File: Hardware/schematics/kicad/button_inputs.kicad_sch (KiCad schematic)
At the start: 28 parts, among them SW1 ENC_A, SW2 ENC_B, SW3 ENC_BUT, SW4 AUTOTUNE_BTN, SW5 OFFSET_RESET, SW6 OFFSET_DISPLAY, SW7 OSC1_THROUGH, SW8 LOAD_SD, U15 74HC595, U16 74HC595, U17 74HC595, U27 74HC165

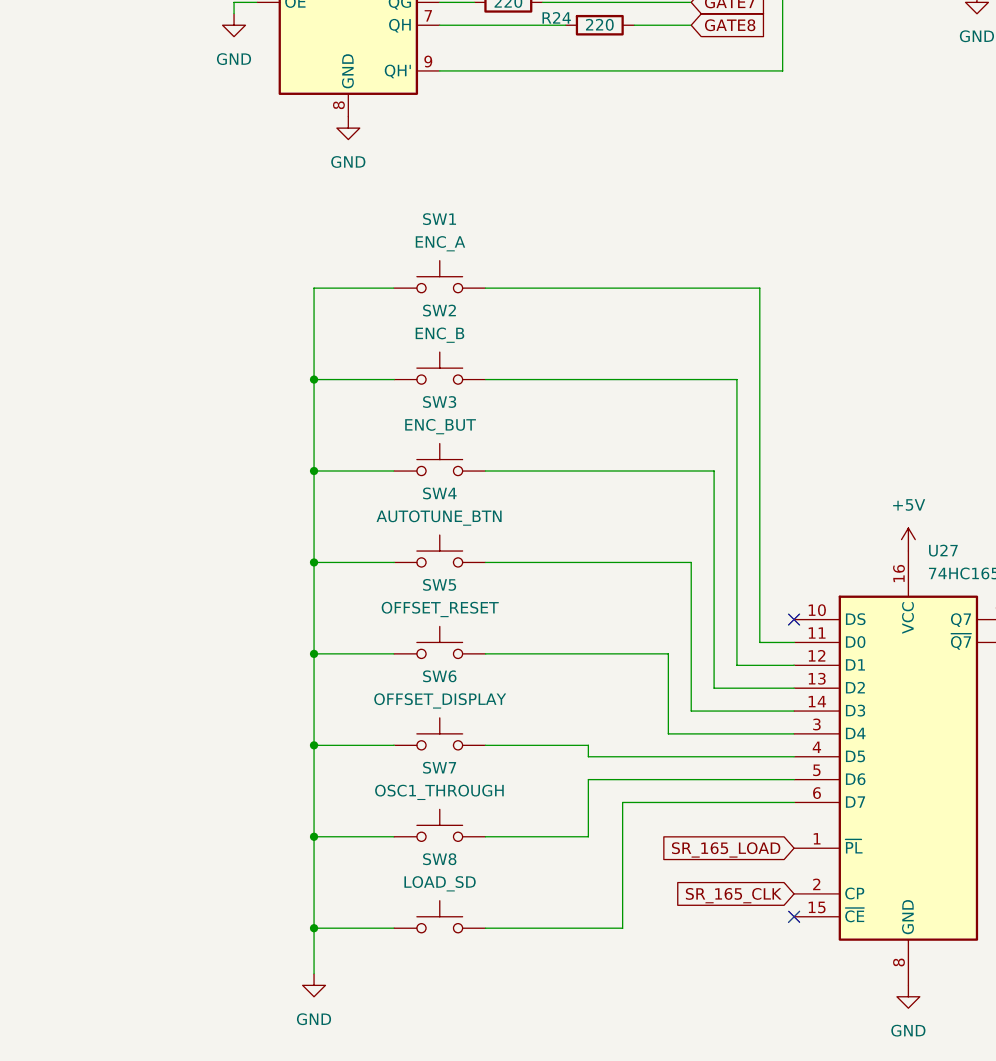
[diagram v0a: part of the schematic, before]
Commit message: Add 3.3v pull-up resistors to buttons
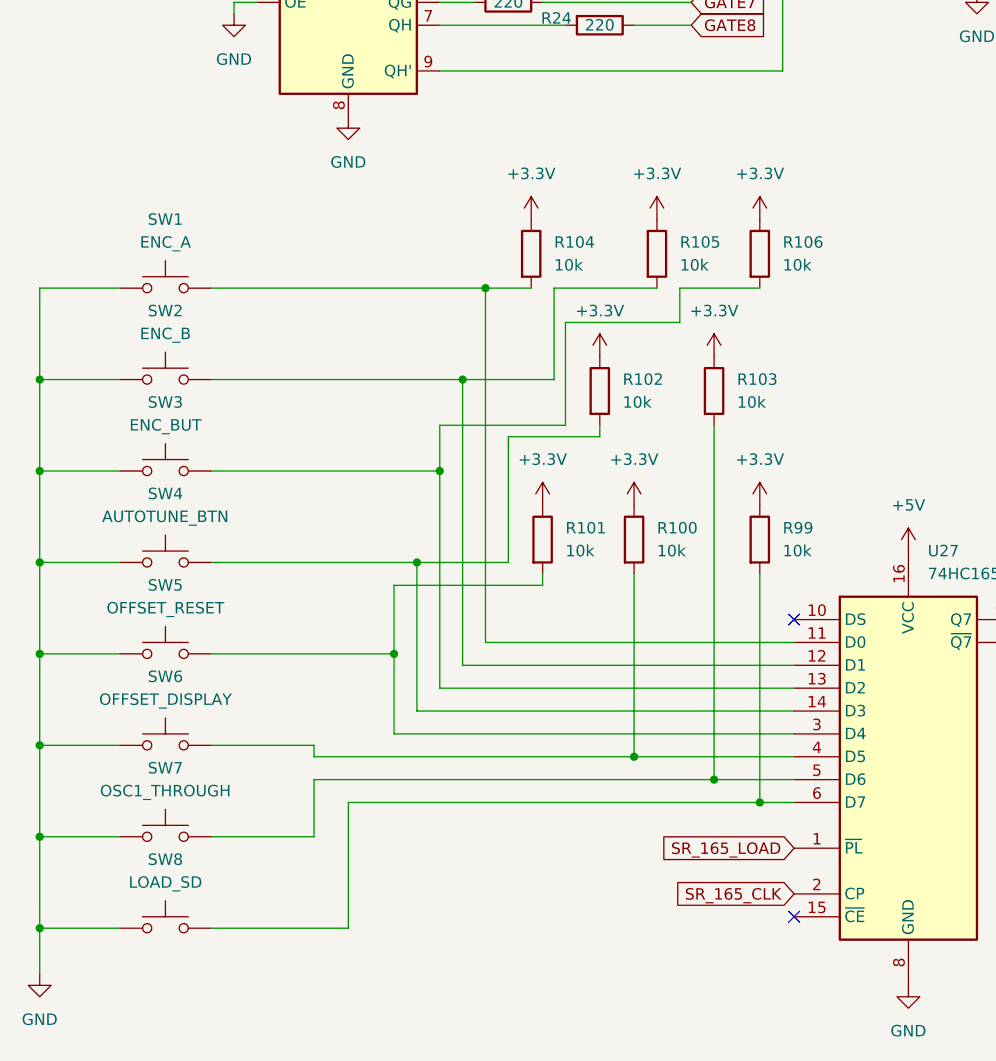
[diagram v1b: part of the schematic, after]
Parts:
- added R100, R101, R102, R103, R104, R105, R106, R99: 10k, symbol Device:R
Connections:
- net at SW1.2, U27.11 (D0): now also R104.2
- net at SW2.2, U27.12 (D1): now also R105.2
- net at SW3.2, U27.13 (D2): now also R106.2
- net at SW4.2, U27.14 (D3): now also R102.2
- net at SW5.2, U27.3 (D4): now also R101.2
- net at SW6.2, U27.4 (D5): now also R100.2
- net at SW7.2, U27.5 (D6): now also R103.2
- net at SW8.2, U27.6 (D7): now also R99.2
- new net +3.3V: R100.1, R101.1, R102.1, R103.1, R104.1, R105.1, R106.1, R99.1
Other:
- moved on the sheet: SW1, SW2, SW3, SW4, SW5, SW6, SW7, SW8

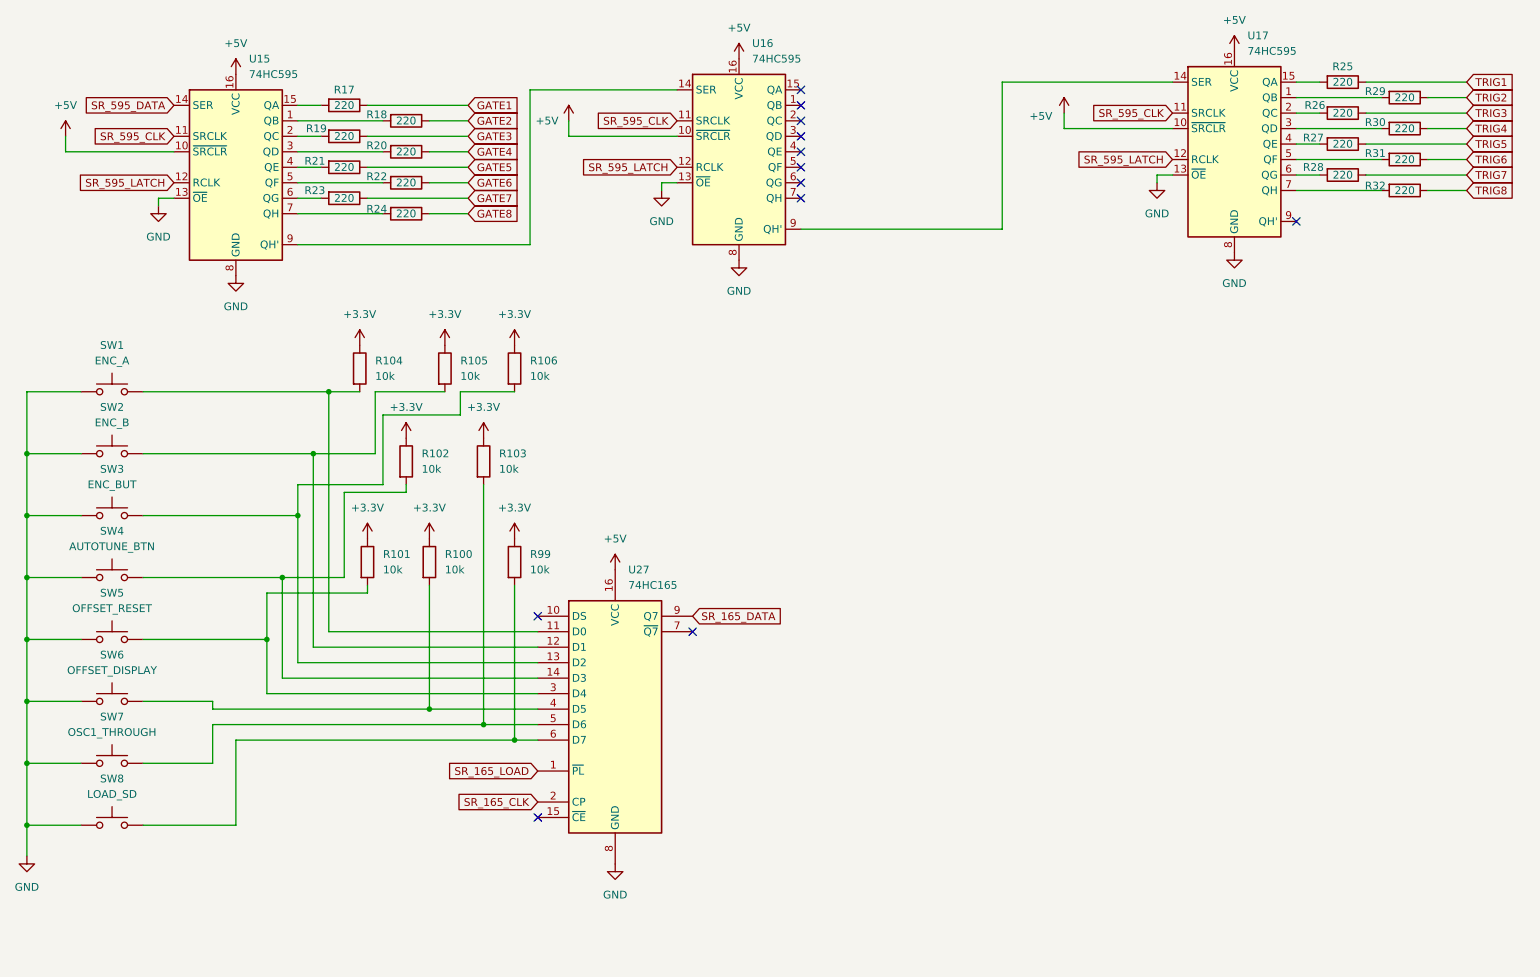
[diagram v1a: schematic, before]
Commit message: Modify schematics to suit a complete Eurorack PCB design
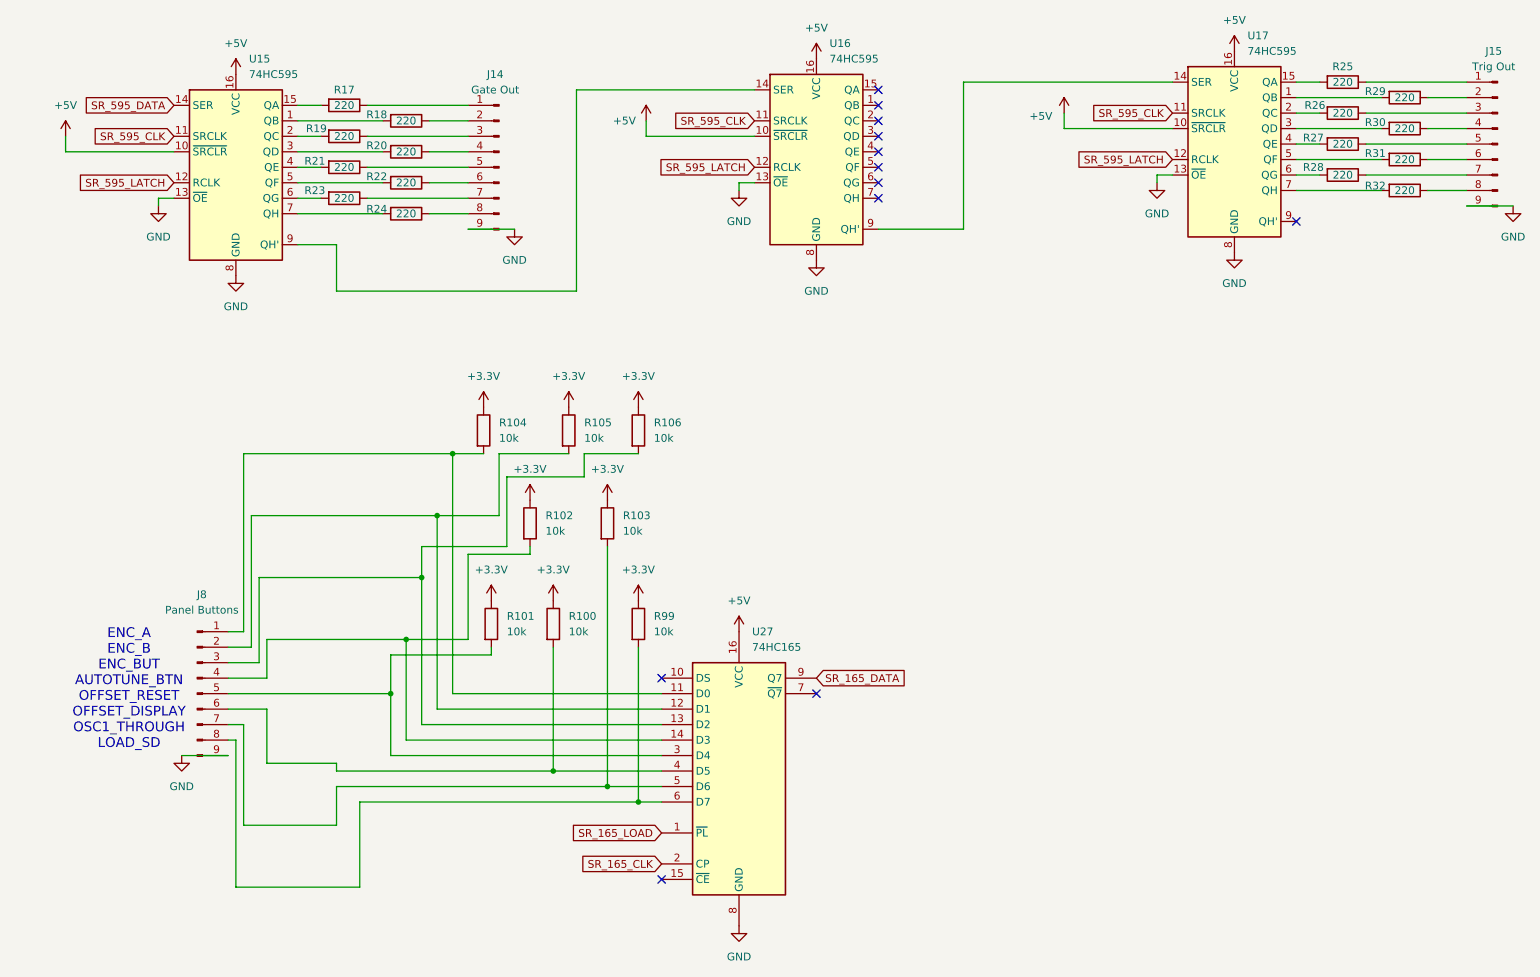
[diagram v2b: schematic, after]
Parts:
- removed SW1: ENC_A, Button_Switch_THT:SW_PUSH_6mm, symbol Switch:SW_Push
- removed SW2: ENC_B, Button_Switch_THT:SW_PUSH_6mm, symbol Switch:SW_Push
- removed SW3: ENC_BUT, Button_Switch_THT:SW_PUSH_6mm, symbol Switch:SW_Push
- removed SW4: AUTOTUNE_BTN, Button_Switch_THT:SW_PUSH_6mm, symbol Switch:SW_Push
- removed SW5: OFFSET_RESET, Button_Switch_THT:SW_PUSH_6mm, symbol Switch:SW_Push
- removed SW6: OFFSET_DISPLAY, Button_Switch_THT:SW_PUSH_6mm, symbol Switch:SW_Push
- removed SW7: OSC1_THROUGH, Button_Switch_THT:SW_PUSH_6mm, symbol Switch:SW_Push
- removed SW8: LOAD_SD, Button_Switch_THT:SW_PUSH_6mm, symbol Switch:SW_Push
- added J14: Gate Out, Connector_JST:JST_XH_B9B-XH-A_1x09_P2.50mm_Vertical, symbol Connector:Conn_01x09_Pin
- added J15: Trig Out, Connector_JST:JST_XH_B9B-XH-A_1x09_P2.50mm_Vertical, symbol Connector:Conn_01x09_Pin
- added J8: Panel Buttons, Connector_JST:JST_XH_B9B-XH-A_1x09_P2.50mm_Vertical, symbol Connector:Conn_01x09_Pin
- R100, R101, R102, R103, R104, R105, R106, R99: footprint (none) -> PCM_Resistor_SMD_AKL:R_0805_2012Metric_Pad1.15x1.40mm_HandSolder
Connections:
- net GND: now also J14.9 (Pin_9), J15.9 (Pin_9), J8.9 (Pin_9)
- net at R104.2, U27.11 (D0): now also J8.1 (Pin_1)
- net at R105.2, U27.12 (D1): now also J8.2 (Pin_2)
- net at R106.2, U27.13 (D2): now also J8.3 (Pin_3)
- net at R102.2, U27.14 (D3): now also J8.4 (Pin_4)
- net at R101.2, U27.3 (D4): now also J8.5 (Pin_5)
- net at R100.2, U27.4 (D5): now also J8.6 (Pin_6)
- net at R103.2, U27.5 (D6): now also J8.7 (Pin_7)
- net at R99.2, U27.6 (D7): now also J8.8 (Pin_8)
- net GATE1: no longer names the net of R17.1
- net GATE1: now also J14.1 (Pin_1)
- net GATE2: no longer names the net of R18.1
- net GATE2: now also J14.2 (Pin_2)
- net GATE3: no longer names the net of R19.1
- net GATE3: now also J14.3 (Pin_3)
- net GATE4: no longer names the net of R20.1
- net GATE4: now also J14.4 (Pin_4)
- net GATE5: no longer names the net of R21.1
- net GATE5: now also J14.5 (Pin_5)
- net GATE6: no longer names the net of R22.1
- net GATE6: now also J14.6 (Pin_6)
- net GATE7: no longer names the net of R23.1
- net GATE7: now also J14.7 (Pin_7)
- net GATE8: no longer names the net of R24.1
- net GATE8: now also J14.8 (Pin_8)
- net TRIG1: no longer names the net of R25.1
- net TRIG1: now also J15.1 (Pin_1)
- net TRIG2: no longer names the net of R29.1
- net TRIG2: now also J15.2 (Pin_2)
- net TRIG3: no longer names the net of R26.1
- net TRIG3: now also J15.3 (Pin_3)
- net TRIG4: no longer names the net of R30.1
- net TRIG4: now also J15.4 (Pin_4)
- net TRIG5: no longer names the net of R27.1
- net TRIG5: now also J15.5 (Pin_5)
- net TRIG6: no longer names the net of R31.1
- net TRIG6: now also J15.6 (Pin_6)
- net TRIG7: no longer names the net of R28.1
- net TRIG7: now also J15.7 (Pin_7)
- net TRIG8: no longer names the net of R32.1
- net TRIG8: now also J15.8 (Pin_8)
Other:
- note added: "ENC_A ENC_B ENC_BUT AUTOTUNE_BTN OFFSET_RESET OFFSET_DISPLAY OSC1_THROUGH LOAD_SD"
- moved on the sheet: R100, R101, R102, R103, R104, R105, R106, R99, U16, U27
